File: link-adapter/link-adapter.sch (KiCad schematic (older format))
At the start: 41 parts, among them J1 ToADC, J2 ToMaster, J3 USB_B, J4 FTDI Header, J5 PowerJumper, J6 CBUS, J7 FORLED, J8 AltUSB, Q1 NX7002BKW, U1 ISL83490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

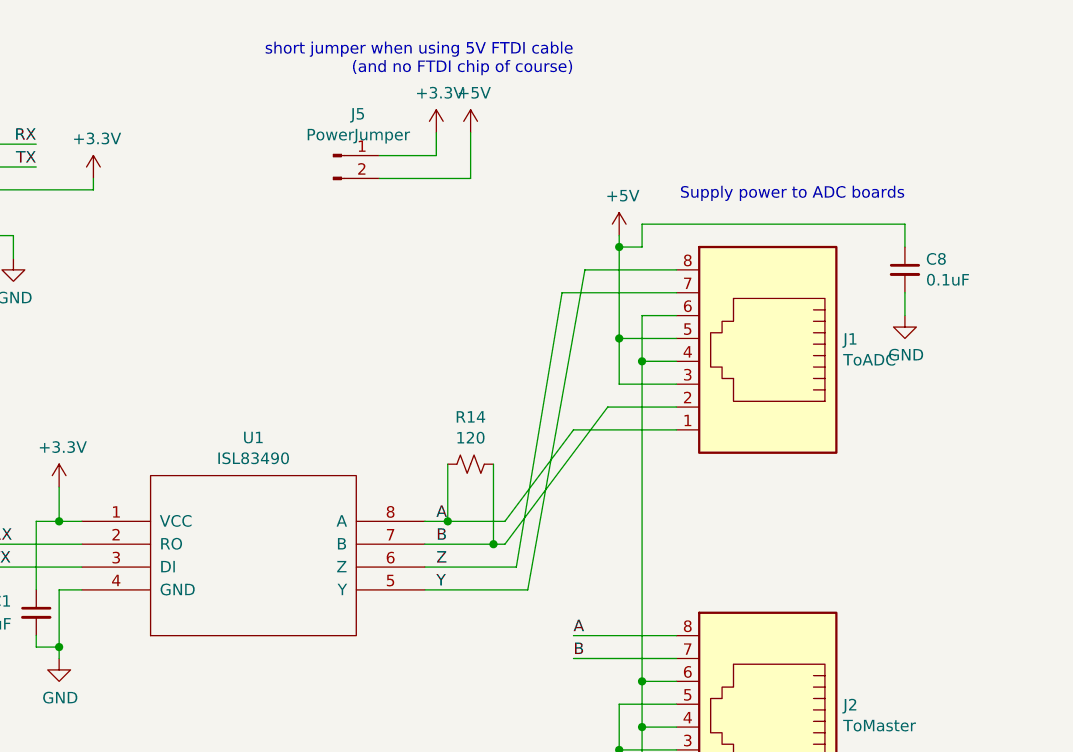
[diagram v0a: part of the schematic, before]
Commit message: include GND in power jumper header so it can receive external power
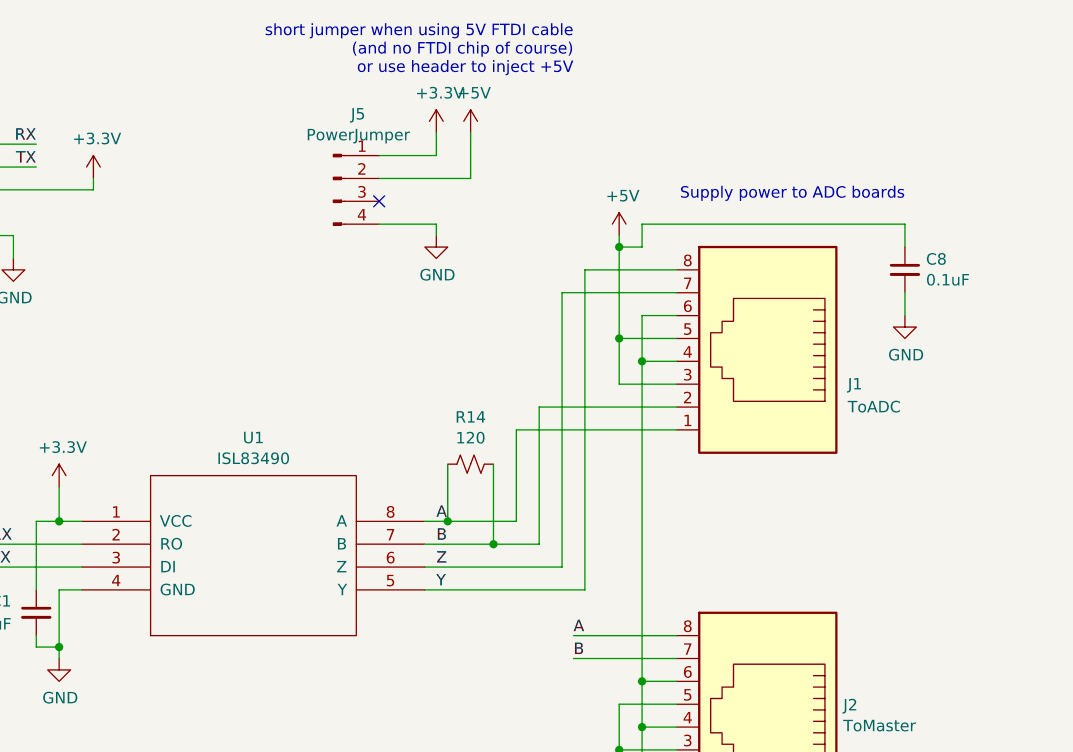
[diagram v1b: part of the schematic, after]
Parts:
- removed J5: PowerJumper, Pin_Headers:Pin_Header_Straight_1x02_Pitch2.54mm, symbol Connector:Conn_01x02_Male
- added J5: PowerJumper, Pin_Headers:Pin_Header_Straight_1x04_Pitch2.54mm, symbol Connector:Conn_01x04_Male
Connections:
- net +3V3: now also J5.1 (Pin_1)
- net +5V: now also J5.2 (Pin_2)
- net GND: now also J5.4 (Pin_4)
- no-connect marks 5 -> 6
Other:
- note added: "short jumper when using 5V FTDI cable\n(and no FTDI chip of course)\nor use header to inject +5V"
- note removed: "short jumper when using 5V FTDI cable\n(and no FTDI chip of course)"
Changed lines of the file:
@@
-	1    0    0    -1
-$EndComp
-$Comp
-L Connector:Conn_01x02_Male J5
-U 1 1 5FB070F2
-P 8100 1350
-F 0 "J5" H 8208 1531 50  0000 C CNN
-F 1 "PowerJumper" H 8208 1440 50  0000 C CNN
-F 2 "Pin_Headers:Pin_Header_Straight_1x02_Pitch2.54mm" H 8100 1350 50  0001 C CNN
-F 3 "~" H 8100 1350 50  0001 C CNN
-	1    8100 1350
 	1    0    0    -1
 $EndComp
@@
 U 1 1 5FB0D205
 P 10000 2250
-F 0 "J1" H 9670 2346 50  0000 R CNN
-F 1 "ToADC" H 9670 2255 50  0000 R CNN
+F 0 "J1" H 9650 2150 50  0000 R CNN
+F 1 "ToADC" H 9650 2050 50  0000 R CNN
 F 2 "Connectors:RJ45_8" V 10000 2275 50  0001 C CNN
 F 3 "~" V 10000 2275 50  0001 C CNN
@@
 Connection ~ 9350 2150
 Wire Wire Line
-	8850 2950 8600 2950
+	8900 2950 8600 2950
 Wire Wire Line
 	8500 3050 8800 3050
 Wire Wire Line
-	8500 3150 8900 3150
-Wire Wire Line
-	8500 3250 8950 3250
+	8500 3150 9100 3150
+Wire Wire Line
+	8500 3250 9200 3250
 Text Notes 10600 1550 2    50   ~ 0
 Supply power to ADC boards
@@
 Connection ~ 9450 3650
 Wire Wire Line
-	9150 2550 9600 2550
-Wire Wire Line
-	9600 2450 9300 2450
+	8900 2550 9600 2550
+Wire Wire Line
+	9600 2450 9000 2450
 Wire Wire Line
 	9200 1850 9600 1850
@@
 $EndComp
 Text Notes 9150 1000 2    50   ~ 0
-short jumper when using 5V FTDI cable\n(and no FTDI chip of course)
+short jumper when using 5V FTDI cable\n(and no FTDI chip of course)\nor use header to inject +5V
 Text Notes 4150 2250 2    50   ~ 0
 Use FT_Prog from FTDI to reprogram for 500mA draw\nand make any other desired changes.
@@
 	9350 1750 9350 2150
 Wire Wire Line
-	9200 1850 8950 3250
-Wire Wire Line
-	8850 2950 9150 2550
-Wire Wire Line
-	8850 3050 9300 2450
-Wire Wire Line
-	8900 3150 9100 1950
+	9200 1850 9200 3250
+Wire Wire Line
+	8900 2950 8900 2550
+Wire Wire Line
+	9000 3050 9000 2450
+Wire Wire Line
+	9100 3150 9100 1950
 Wire Wire Line
 	9150 3550 9600 3550
@@
 Connection ~ 8800 3050
 Wire Wire Line
-	8800 3050 8850 3050
+	8800 3050 9000 3050
+$Comp
+L Connector:Conn_01x04_Male J5
+U 1 1 5FB79CB6
+P 8100 1450
+F 0 "J5" H 8208 1731 50  0000 C CNN
+F 1 "PowerJumper" H 8208 1640 50  0000 C CNN
+F 2 "Pin_Headers:Pin_Header_Straight_1x04_Pitch2.54mm" H 8100 1450 50  0001 C CNN
+F 3 "~" H 8100 1450 50  0001 C CNN
+	1    8100 1450
+	1    0    0    -1
+$EndComp
+NoConn ~ 8300 1550
+Wire Wire Line
+	8300 1650 8550 1650
+Wire Wire Line
+	8550 1650 8550 1700
+$Comp
+L power:GND #PWR0128
+U 1 1 5FB95E11
+P 8550 1700
+F 0 "#PWR0128" H 8550 1450 50  0001 C CNN
+F 1 "GND" H 8555 1527 50  0000 C CNN
+F 2 "" H 8550 1700 50  0001 C CNN
+F 3 "" H 8550 1700 50  0001 C CNN
+	1    8550 1700
+	1    0    0    -1
+$EndComp
 $EndSCHEMATC

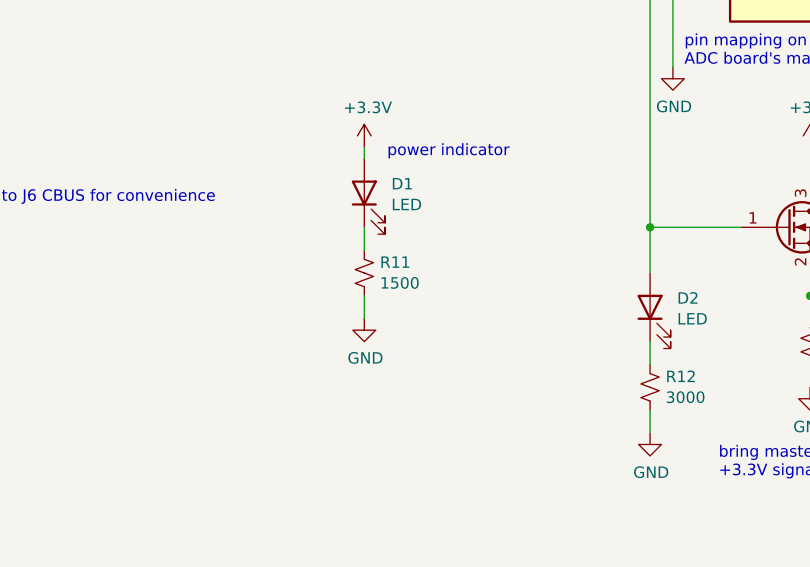
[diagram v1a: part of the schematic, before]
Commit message: fix missing ground in rev0; adjust silk screen for readability
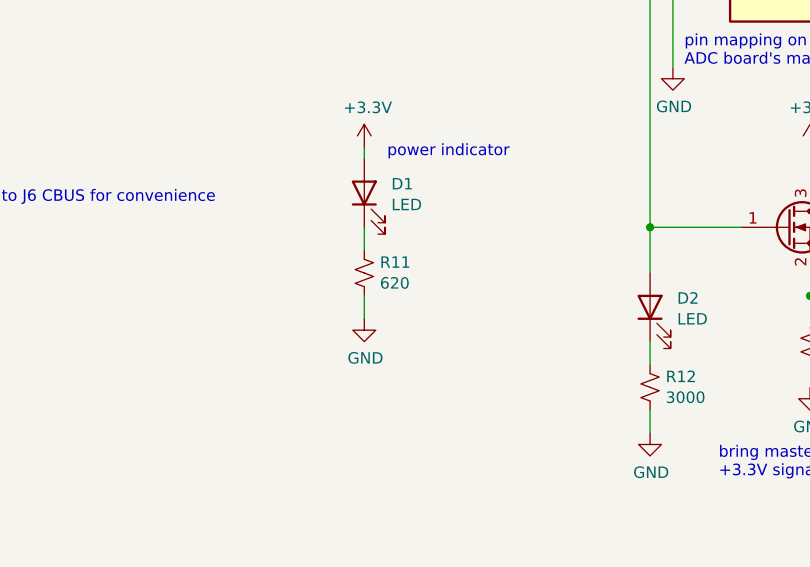
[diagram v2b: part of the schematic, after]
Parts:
- R11: value 1500 -> 620
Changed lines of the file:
@@
 P 8100 5350
 F 0 "R11" H 8168 5396 50  0000 L CNN
-F 1 "1500" H 8168 5305 50  0000 L CNN
+F 1 "620" H 8168 5305 50  0000 L CNN
 F 2 "Resistors_SMD:R_0805_HandSoldering" H 8100 5350 50  0001 C CNN
 F 3 "~" H 8100 5350 50  0001 C CNN

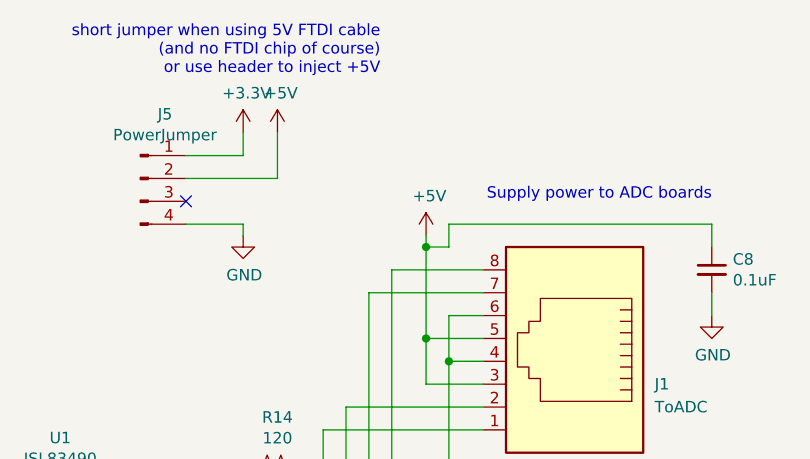
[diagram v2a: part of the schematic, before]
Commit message: Add a header for measuring current to ADC board
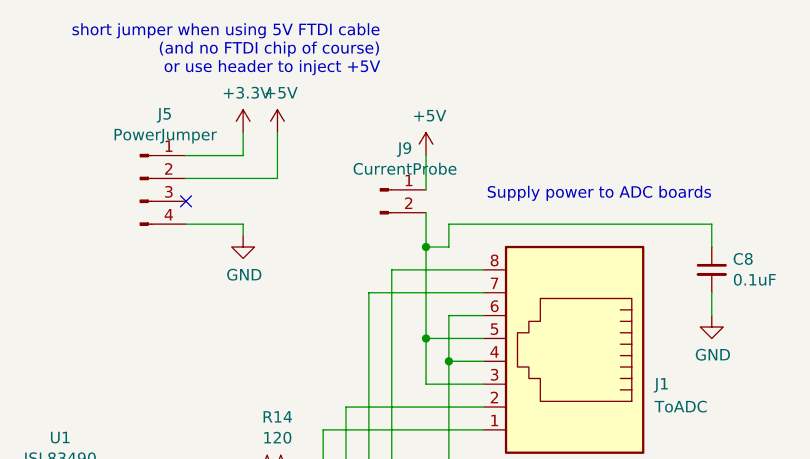
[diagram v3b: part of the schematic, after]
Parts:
- added J9: CurrentProbe, Pin_Headers:Pin_Header_Straight_1x02_Pitch2.54mm, symbol Connector:Conn_01x02_Male
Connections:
- net +5V: now also J9.1 (Pin_1); no longer C8.1, J1.3, J1.5
- new net: C8.1, J1.3, J1.5, J9.2 (Pin_2)
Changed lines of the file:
@@
 L power:+5V #PWR0112
 U 1 1 5FB16EF9
-P 9350 1700
-F 0 "#PWR0112" H 9350 1550 50  0001 C CNN
-F 1 "+5V" H 9365 1873 50  0000 C CNN
-F 2 "" H 9350 1700 50  0001 C CNN
-F 3 "" H 9350 1700 50  0001 C CNN
-	1    9350 1700
+P 9350 1350
+F 0 "#PWR0112" H 9350 1200 50  0001 C CNN
+F 1 "+5V" H 9365 1523 50  0000 C CNN
+F 2 "" H 9350 1350 50  0001 C CNN
+F 3 "" H 9350 1350 50  0001 C CNN
+	1    9350 1350
 	1    0    0    -1
 $EndComp
@@
 bring master power line down to a\n+3.3V signal for FT230XS GPIO
 Wire Wire Line
-	9350 1700 9350 1750
-Wire Wire Line
 	10600 1650 10600 1750
 Wire Wire Line
@@
 	1    0    0    -1
 $EndComp
+$Comp
+L Connector:Conn_01x02_Male J9
+U 1 1 5FCCBCDB
+P 9150 1500
+F 0 "J9" H 9258 1681 50  0000 C CNN
+F 1 "CurrentProbe" H 9258 1590 50  0000 C CNN
+F 2 "Pin_Headers:Pin_Header_Straight_1x02_Pitch2.54mm" H 9150 1500 50  0001 C CNN
+F 3 "~" H 9150 1500 50  0001 C CNN
+	1    9150 1500
+	1    0    0    -1
+$EndComp
+Wire Wire Line
+	9350 1600 9350 1750
+Wire Wire Line
+	9350 1500 9350 1350
 $EndSCHEMATC

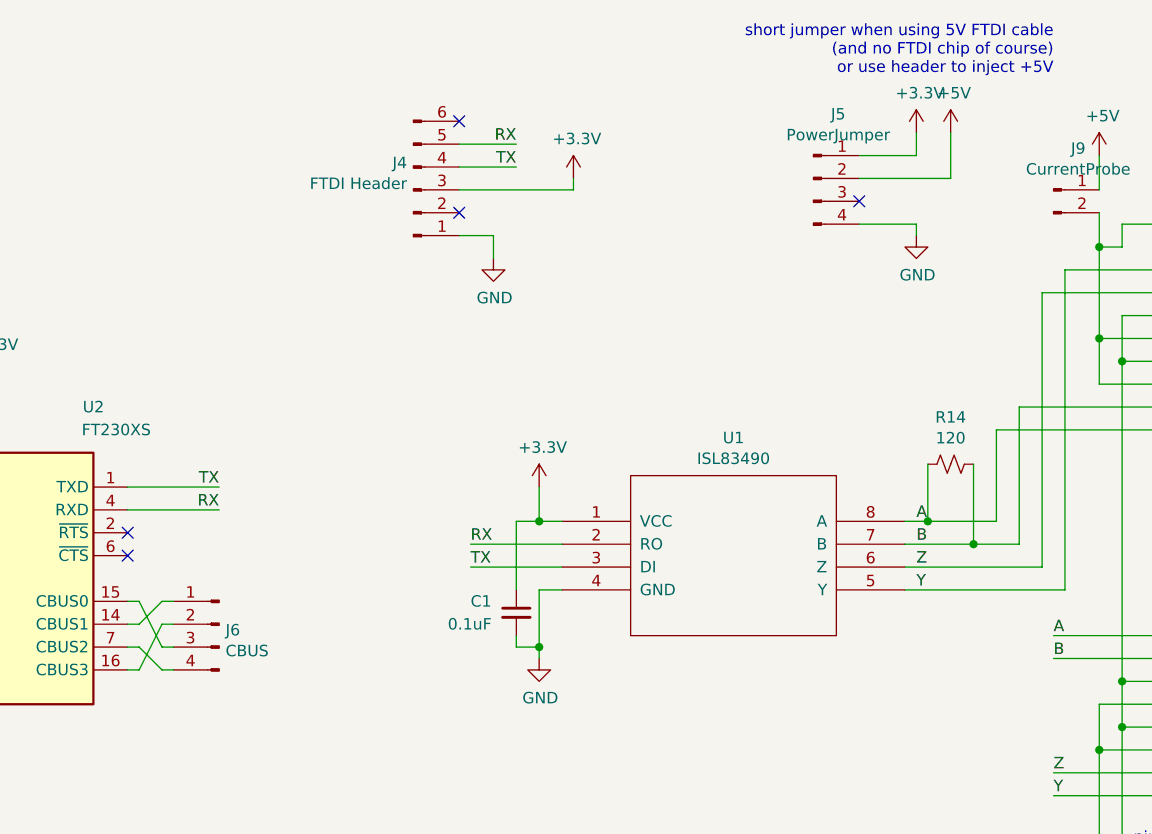
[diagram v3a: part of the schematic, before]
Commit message: Silkscreen improvements for usability
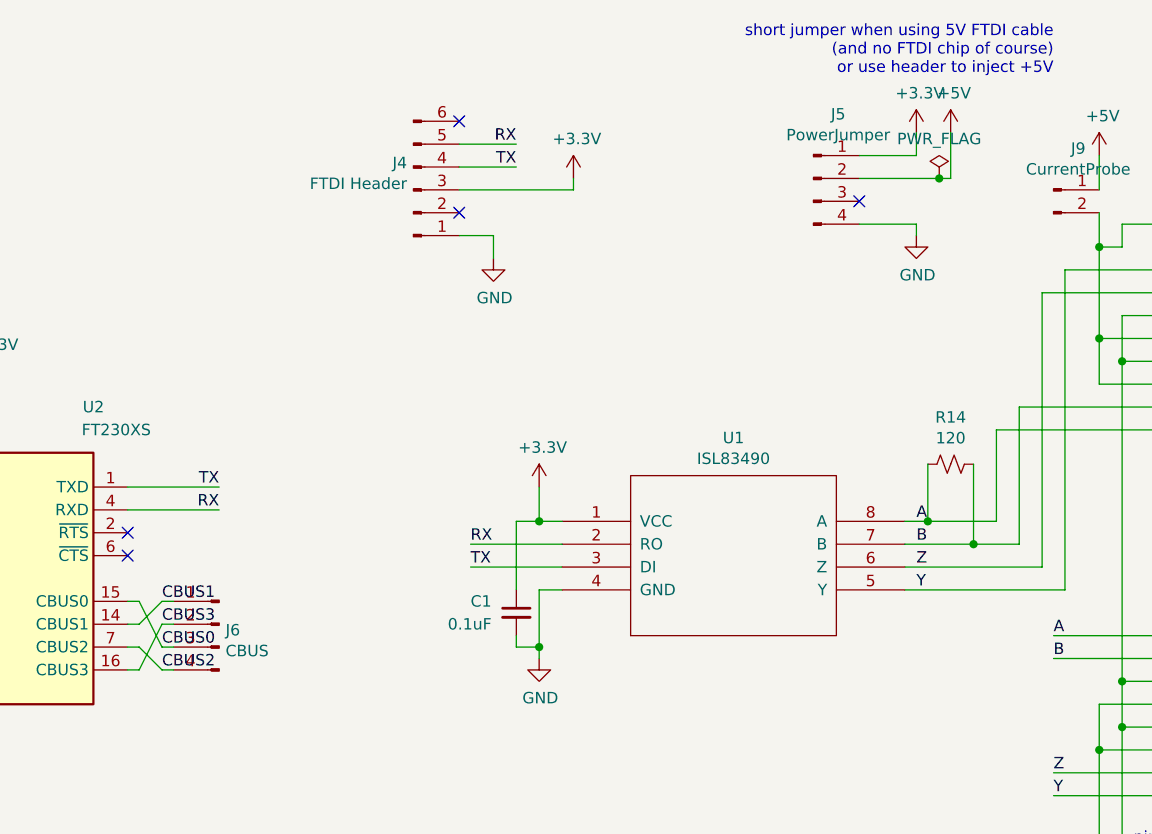
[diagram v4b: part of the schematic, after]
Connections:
- net CBUS1: now reaches J6.1 (Pin_1), U2.14 (CBUS1)
- net CBUS0: now reaches J6.3 (Pin_3), U2.15 (CBUS0)
- net CBUS3: now reaches J6.2 (Pin_2), U2.16 (CBUS3)
- net CBUS2: now reaches J6.4 (Pin_4), U2.7 (CBUS2)
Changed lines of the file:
@@
 	8550 1350 8550 1250
 Wire Wire Line
-	8300 1450 8700 1450
+	8300 1450 8650 1450
 Wire Wire Line
 	8700 1450 8700 1250
@@
 Wire Wire Line
 	9350 1500 9350 1350
+$Comp
+L power:PWR_FLAG #FLG0101
+U 1 1 5FDF6D1C
+P 8650 1450
+F 0 "#FLG0101" H 8650 1525 50  0001 C CNN
+F 1 "PWR_FLAG" H 8650 1623 50  0000 C CNN
+F 2 "" H 8650 1450 50  0001 C CNN
+F 3 "~" H 8650 1450 50  0001 C CNN
+	1    8650 1450
+	1    0    0    -1
+$EndComp
+Connection ~ 8650 1450
+Wire Wire Line
+	8650 1450 8700 1450
+Text Label 5250 3300 0    50   ~ 0
+CBUS1
+Text Label 5250 3500 0    50   ~ 0
+CBUS0
+Text Label 5250 3400 0    50   ~ 0
+CBUS3
+Text Label 5250 3600 0    50   ~ 0
+CBUS2
 $EndSCHEMATC
